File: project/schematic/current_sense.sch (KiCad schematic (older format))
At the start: 6 parts

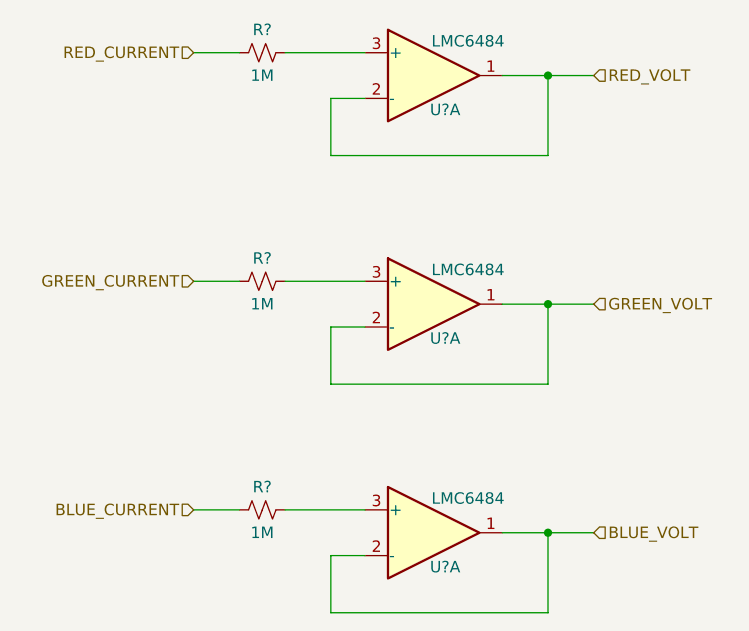
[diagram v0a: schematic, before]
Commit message: switch to high pass filters
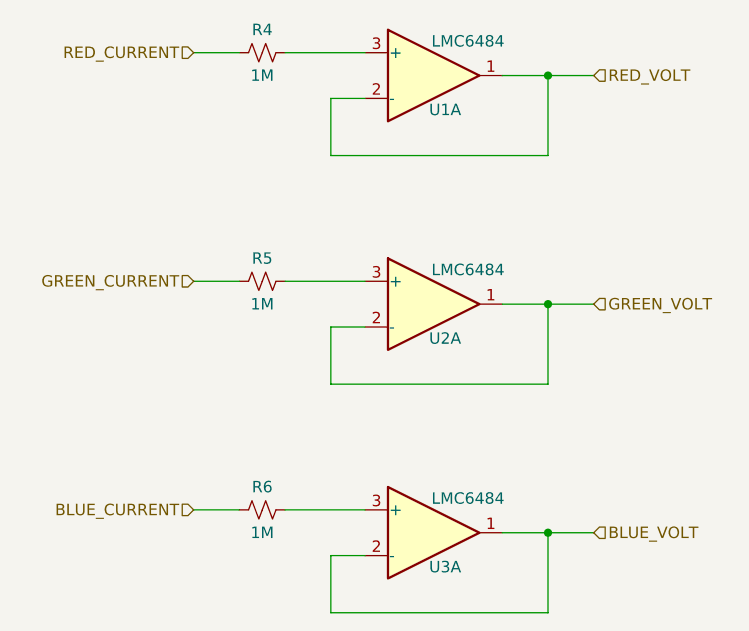
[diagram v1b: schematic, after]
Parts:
- gave numbers to parts that had none: 6
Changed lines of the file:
@@
 EESchema Schematic File Version 4
+LIBS:final_project_schematic-cache
 EELAYER 30 0
 EELAYER END
@@
 	4650 2600 4850 2600
 $Comp
-L Device:R_Small_US R?
+L Device:R_Small_US R4
 U 1 1 5E47CFED
 P 4950 2600
-F 0 "R?" V 4850 2600 50  0000 C CNN
+F 0 "R4" V 4850 2600 50  0000 C CNN
 F 1 "1M" V 5050 2600 50  0000 C CNN
 F 2 "" H 4950 2600 50  0001 C CNN
@@
 AR Path="/5E481FE1" Ref="U?"  Part="1"
 AR Path="/5E40D9B5/5E481FE1" Ref="U?"  Part="1"
-AR Path="/5E46A20A/5E481FE1" Ref="U?"  Part="1"
-F 0 "U?" H 5750 2550 50  0000 C CNN
+AR Path="/5E46A20A/5E481FE1" Ref="U1"  Part="1"
+F 0 "U1" H 5750 2550 50  0000 C CNN
 F 1 "LMC6484" H 5850 2850 50  0000 C CNN
 F 2 "" H 5700 2700 50  0001 C CNN
@@
 	4650 3600 4850 3600
 $Comp
-L Device:R_Small_US R?
+L Device:R_Small_US R5
 U 1 1 5E4941C0
 P 4950 3600
-F 0 "R?" V 4850 3600 50  0000 C CNN
+F 0 "R5" V 4850 3600 50  0000 C CNN
 F 1 "1M" V 5050 3600 50  0000 C CNN
 F 2 "" H 4950 3600 50  0001 C CNN
@@
 AR Path="/5E4941C6" Ref="U?"  Part="1"
 AR Path="/5E40D9B5/5E4941C6" Ref="U?"  Part="1"
-AR Path="/5E46A20A/5E4941C6" Ref="U?"  Part="1"
-F 0 "U?" H 5750 3550 50  0000 C CNN
+AR Path="/5E46A20A/5E4941C6" Ref="U2"  Part="1"
+F 0 "U2" H 5750 3550 50  0000 C CNN
 F 1 "LMC6484" H 5850 3850 50  0000 C CNN
 F 2 "" H 5700 3700 50  0001 C CNN
@@
 	4650 4600 4850 4600
 $Comp
-L Device:R_Small_US R?
+L Device:R_Small_US R6
 U 1 1 5E497F57
 P 4950 4600
-F 0 "R?" V 4850 4600 50  0000 C CNN
+F 0 "R6" V 4850 4600 50  0000 C CNN
 F 1 "1M" V 5050 4600 50  0000 C CNN
 F 2 "" H 4950 4600 50  0001 C CNN
@@
 AR Path="/5E497F5D" Ref="U?"  Part="1"
 AR Path="/5E40D9B5/5E497F5D" Ref="U?"  Part="1"
-AR Path="/5E46A20A/5E497F5D" Ref="U?"  Part="1"
-F 0 "U?" H 5750 4550 50  0000 C CNN
+AR Path="/5E46A20A/5E497F5D" Ref="U3"  Part="1"
+F 0 "U3" H 5750 4550 50  0000 C CNN
 F 1 "LMC6484" H 5850 4850 50  0000 C CNN
 F 2 "" H 5700 4700 50  0001 C CNN
